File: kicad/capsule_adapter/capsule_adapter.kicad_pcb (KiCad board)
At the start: 2 copper layers, 19 x 7.1 mm, 4 parts

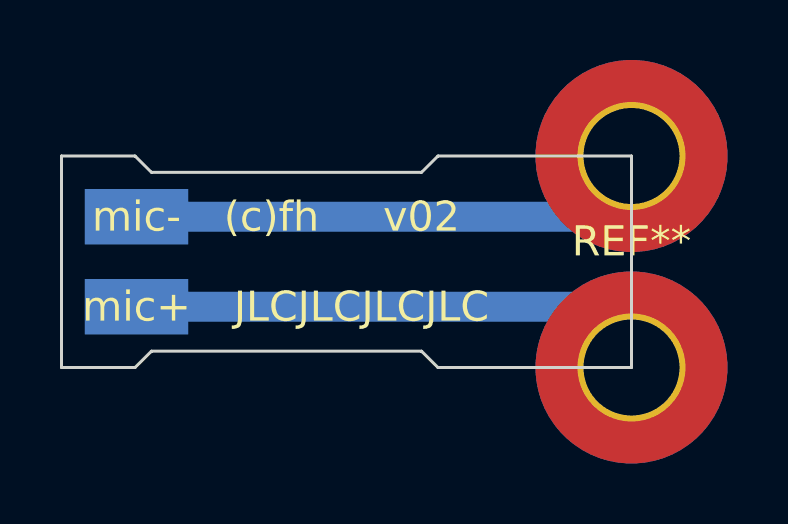
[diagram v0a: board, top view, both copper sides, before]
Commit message: fixed silk at mounting holes
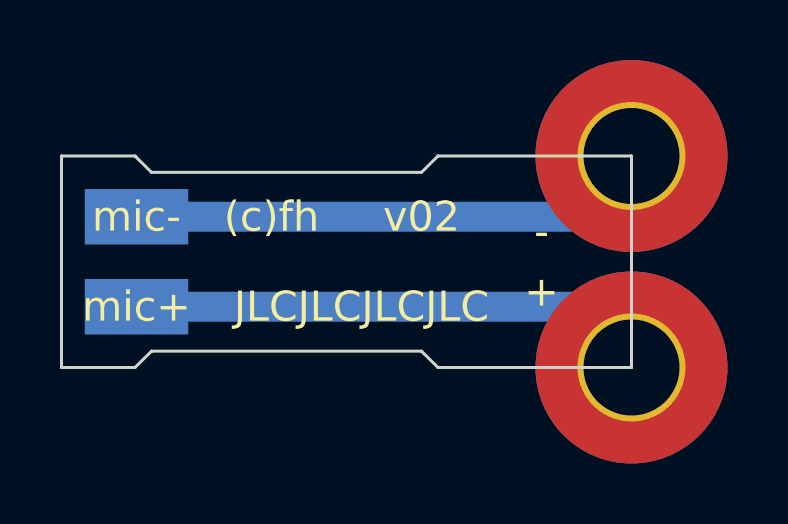
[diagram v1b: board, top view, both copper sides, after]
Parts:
- renumbered REF** to +, REF** to -
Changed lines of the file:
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@@
     (tags "mounting hole 3.2mm m3")
     (attr exclude_from_pos_files exclude_from_bom)
-    (fp_text reference "REF**" (at 0 -4.2) (layer "F.SilkS")
+    (fp_text reference "+" (at -3 -2.525) (layer "F.SilkS")
       (effects (font (size 1 1) (thickness 0.15)))
     )
@@
     (tags "mounting hole 3.2mm m3")
     (attr exclude_from_pos_files exclude_from_bom)
-    (fp_text reference "REF**" (at 0 4.2) (layer "B.SilkS")
-      (effects (font (size 1 1) (thickness 0.15)) (justify mirror))
+    (fp_text reference "-" (at 3 -2.525) (layer "F.SilkS")
+      (effects (font (size 1 1) (thickness 0.15)))
     )
     (fp_text value "MountingHole_3.2mm_M3_Pad_TopBottom" (at 0 -4.2) (layer "B.Fab")

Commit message: small updates and new readme
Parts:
- +: renamed from -; moved to F.Cu
- turned + to 0 degrees
- renumbered - to +, + to -
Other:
- board text added: "diy_mm"
- board text removed: "(c)fh"
- board text removed: "JLCJLCJLCJLC"
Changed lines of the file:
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@@
   )
   (paper "A4")
+  (title_block
+    (title "capsule_adapter")
+    (date "2022-02-05")
+    (rev "v02")
+    (company "Author: felhub")
+  )
   (layers
     (0 "F.Cu" signal)
@@
       (layerselection 0x00010fc_ffffffff)
       (disableapertmacros false)
-      (usegerberextensions false)
+      (usegerberextensions true)
       (usegerberattributes true)
-      (usegerberadvancedattributes true)
+      (usegerberadvancedattributes false)
       (creategerberjobfile true)
       (svguseinch false)
@@
       (plotinvisibletext false)
       (sketchpadsonfab false)
-      (subtractmaskfromsilk false)
+      (subtractmaskfromsilk true)
       (outputformat 1)
       (mirror false)
-      (drillshape 1)
+      (drillshape 0)
       (scaleselection 1)
-      (outputdirectory "")
+      (outputdirectory "X:/TUWien/Akustik/diy_mm/kicad/capsule_adapter/gerbers/")
     )
   )
@@
     (tags "mounting hole 3.2mm m3")
     (attr exclude_from_pos_files exclude_from_bom)
-    (fp_text reference "+" (at -3 -2.525) (layer "F.SilkS")
+    (fp_text reference "-" (at -3 -2.525) (layer "F.SilkS") hide
       (effects (font (size 1 1) (thickness 0.15)))
     )
-    (fp_text value "MountingHole_3.2mm_M3_Pad_TopBottom" (at 0 4.2) (layer "F.Fab")
-      (effects (font (size 1 1) (thickness 0.15)))
-    )
-    (fp_text user "${REFERENCE}" (at 0.3 0) (layer "F.Fab")
-      (effects (font (size 1 1) (thickness 0.15)))
+    (fp_text value "MountingHole_3.2mm_M3_Pad_TopBottom" (at 0 3.975) (layer "B.Fab")
+      (effects (font (size 1 1) (thickness 0.15)) (justify mirror))
+    )
+    (fp_text user "${REFERENCE}" (at 0.3 0) (layer "B.Fab")
+      (effects (font (size 1 1) (thickness 0.15)) (justify mirror))
     )
     (fp_circle (center 0 0) (end 3.2 0) (layer "Cmts.User") (width 0.15) (fill none))
@@
     (pad "1" thru_hole circle locked (at 0 0) (size 3.6 3.6) (drill 3.2) (layers *.Cu *.Mask))
   )
-  (footprint "MountingHole:MountingHole_3.2mm_M3_Pad_TopBottom" (layer "B.Cu")
-    (at 119 96.475 180)
+  (footprint "MountingHole:MountingHole_3.2mm_M3_Pad_TopBottom" (layer "F.Cu")
+    (at 119 96.475)
     (descr "Mounting Hole 3.2mm, M3")
     (tags "mounting hole 3.2mm m3")
     (attr exclude_from_pos_files exclude_from_bom)
-    (fp_text reference "-" (at 3 -2.525) (layer "F.SilkS")
+    (fp_text reference "+" (at 3 2.525) (layer "F.SilkS") hide
       (effects (font (size 1 1) (thickness 0.15)))
     )
-    (fp_text value "MountingHole_3.2mm_M3_Pad_TopBottom" (at 0 -4.2) (layer "B.Fab")
+    (fp_text value "MountingHole_3.2mm_M3_Pad_TopBottom" (at 0 -3.975) (layer "B.Fab")
       (effects (font (size 1 1) (thickness 0.15)) (justify mirror))
     )
@@
     )
     (fp_circle (center 0 0) (end 3.2 0) (layer "Cmts.User") (width 0.15) (fill none))
-    (fp_circle (center 0 0) (end 3.45 0) (layer "B.CrtYd") (width 0.05) (fill none))
-    (pad "1" connect circle locked (at 0 0 180) (size 6.4 6.4) (layers "B.Cu" "B.Mask"))
-    (pad "1" thru_hole circle locked (at 0 0 180) (size 3.6 3.6) (drill 3.2) (layers *.Cu *.Mask))
-    (pad "1" connect circle locked (at 0 0 180) (size 6.4 6.4) (layers "F.Cu" "F.Mask"))
+    (fp_circle (center 0 0) (end 3.45 0) (layer "F.CrtYd") (width 0.05) (fill none))
+    (pad "1" connect circle locked (at 0 0) (size 6.4 6.4) (layers "F.Cu" "F.Mask"))
+    (pad "1" thru_hole circle locked (at 0 0) (size 3.6 3.6) (drill 3.2) (layers *.Cu *.Mask))
+    (pad "1" connect circle locked (at 0 0) (size 6.4 6.4) (layers "B.Cu" "B.Mask"))
   )
   (footprint "digikey-footprints:PC_TEST_POINT_SMD" (layer "B.Cu")
     (at 102.5 98.5 180)
     (attr smd)
-    (fp_text reference "-" (at -3 0) (layer "B.SilkS")
-      (effects (font (size 1 1) (thickness 0.15)) (justify mirror))
-    )
-    (fp_text value "PC_TEST_POINT_SMD" (at 0 -2.02) (layer "B.Fab")
+    (fp_text reference "+" (at -3 0) (layer "B.SilkS") hide
+      (effects (font (size 1 1) (thickness 0.15)) (justify mirror))
+    )
+    (fp_text value "PC_TEST_POINT_SMD" (at 0 3) (layer "B.Fab")
+      (effects (font (size 1 1) (thickness 0.15)) (justify mirror))
+    )
+    (fp_text user "+" (at -3 0 180 unlocked) (layer "B.SilkS")
       (effects (font (size 1 1) (thickness 0.15)) (justify mirror))
     )
@@
     (at 102.5 101.5 180)
     (attr smd)
-    (fp_text reference "+" (at -3 0) (layer "B.SilkS")
-      (effects (font (size 1 1) (thickness 0.15)) (justify mirror))
-    )
-    (fp_text value "PC_TEST_POINT_SMD" (at 0 -2.02) (layer "B.Fab")
+    (fp_text reference "-" (at -3 0) (layer "B.SilkS") hide
+      (effects (font (size 1 1) (thickness 0.15)) (justify mirror))
+    )
+    (fp_text value "PC_TEST_POINT_SMD" (at 0 -3) (layer "B.Fab")
+      (effects (font (size 1 1) (thickness 0.15)) (justify mirror))
+    )
+    (fp_text user "-" (at -3 0 180 unlocked) (layer "B.SilkS")
       (effects (font (size 1 1) (thickness 0.15)) (justify mirror))
     )
@@
   (gr_line (start 100 96.475) (end 100 103.525) (layer "Edge.Cuts") (width 0.1))
   (gr_line (start 102.45 96.475) (end 103 97.02) (layer "Edge.Cuts") (width 0.1))
-  (gr_text "(c)fh" (at 107 98.5) (layer "F.SilkS")
-    (effects (font (size 1 1) (thickness 0.15)))
-  )
-  (gr_text "mic-" (at 102.5 98.5) (layer "F.SilkS")
-    (effects (font (size 1 1) (thickness 0.15)))
-  )
-  (gr_text "JLCJLCJLCJLC" (at 110 101.5) (layer "F.SilkS")
-    (effects (font (size 1 1) (thickness 0.15)))
-  )
-  (gr_text "mic+" (at 102.5 101.5) (layer "F.SilkS")
-    (effects (font (size 1 1) (thickness 0.15)))
-  )
-  (gr_text "v02" (at 112 98.5) (layer "F.SilkS")
-    (effects (font (size 1 1) (thickness 0.15)))
-  )
+  (gr_text "diy_mm" (at 108 101.5) (layer "F.SilkS")
+    (effects (font (size 1 1) (thickness 0.15)))
+  )
+  (gr_text "mic+" (at 102.5 98.5) (layer "F.SilkS")
+    (effects (font (size 1 1) (thickness 0.15)))
+  )
+  (gr_text "mic-" (at 102.5 101.5) (layer "F.SilkS")
+    (effects (font (size 1 1) (thickness 0.15)))
+  )
+  (gr_text "v02" (at 113 101.5) (layer "F.SilkS")
+    (effects (font (size 1 1) (thickness 0.15)))
+  )
